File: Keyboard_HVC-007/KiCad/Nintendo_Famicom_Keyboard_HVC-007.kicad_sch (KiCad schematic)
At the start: 96 parts, among them J1 READ/EAR, J2 Conn_01x15, J3 WRITE/MIC, SW1 F8, SW10 @, SW11 ;, SW12 :, SW13 ン, SW14 /, SW15 -, SW16 ^, SW17 F6, SW18 O, SW19 L, SW2 RET, SW20 K, SW21 ,, SW22 ., SW23 P, SW24 0, SW25 F5, SW26 I, SW27 U, SW28 J, SW29 M, SW3 [, SW30 N, SW31 9, SW32 8, SW33 F4, SW34 Y, SW35 G, SW36 H, SW37 B, SW38 V, SW39 7, SW4 ], SW40 6, SW41 F3, SW42 T, SW43 R, SW44 D, SW45 F, SW46 C, SW47 5, SW48 4, SW49 F2, SW5 カナ, SW50 W, SW51 S, SW52 A, SW53 X, SW54 Z, SW55 E, SW56 3, SW57 F1, SW58 ESC, SW59 Q, SW6 RH SHIFT, SW60 CTR, SW61 LH SHIFT, SW62 GRPH, SW63 1, SW64 2, SW65 CLR HOME, SW66 UP, SW67 RIGHT, SW68 LEFT, SW69 DOWN, SW7 ￥, SW70 SPACE, SW71 DEL, SW72 INS, SW8 STOP, SW9 F7, U1 4017, U2 4019, U3 4069

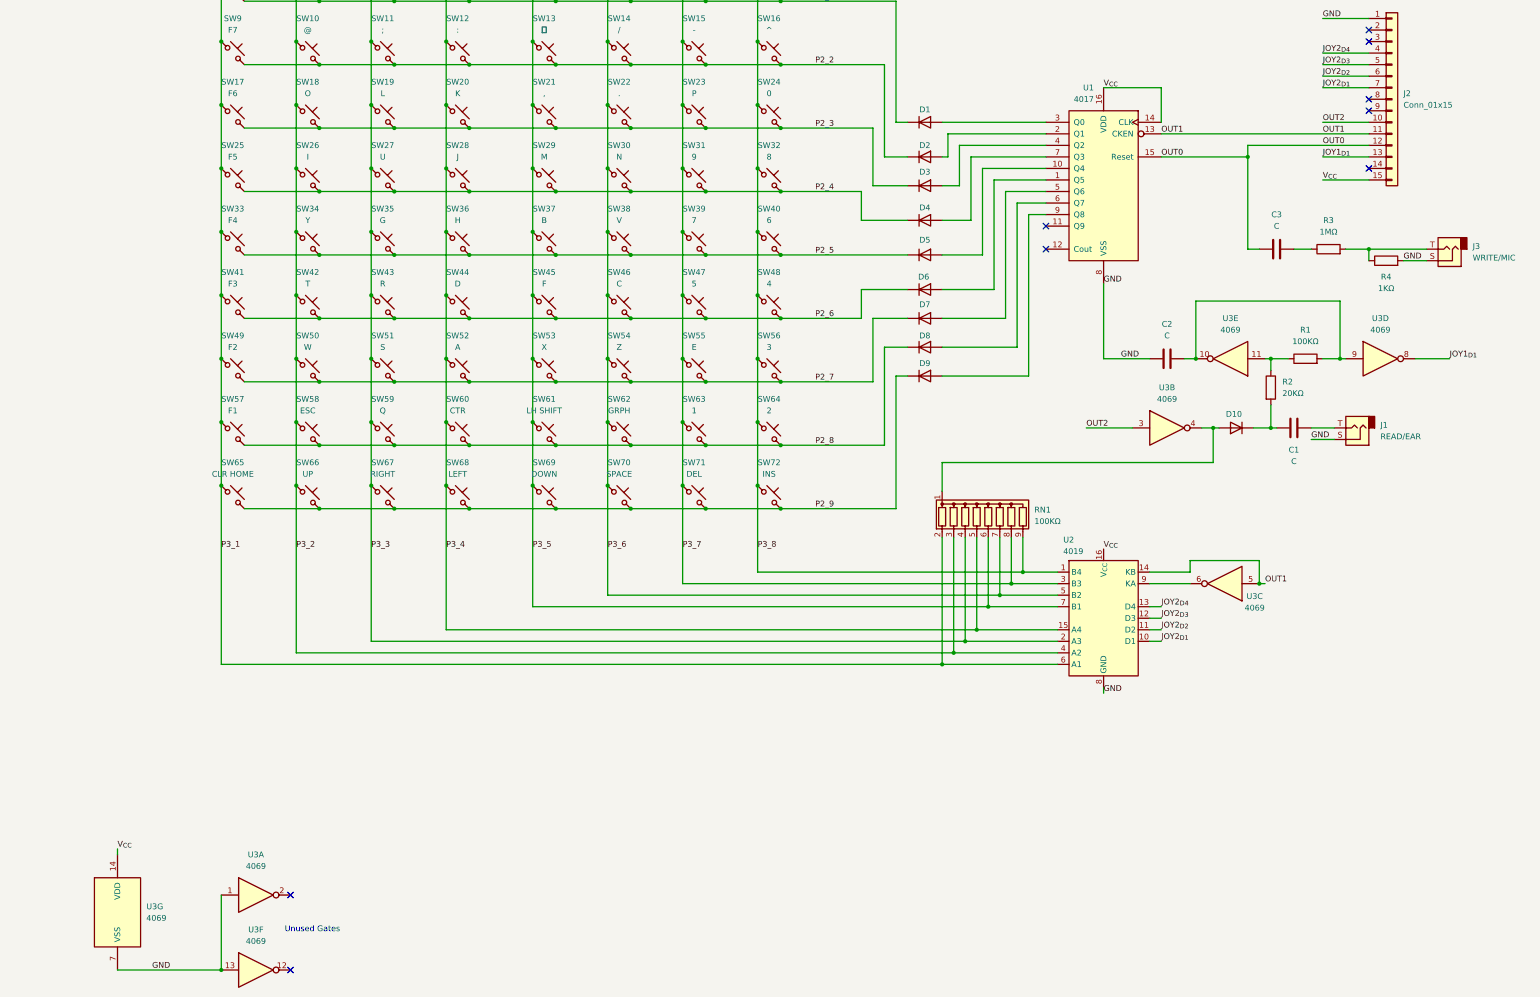
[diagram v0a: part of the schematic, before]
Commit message: Initial keyboard schematic done
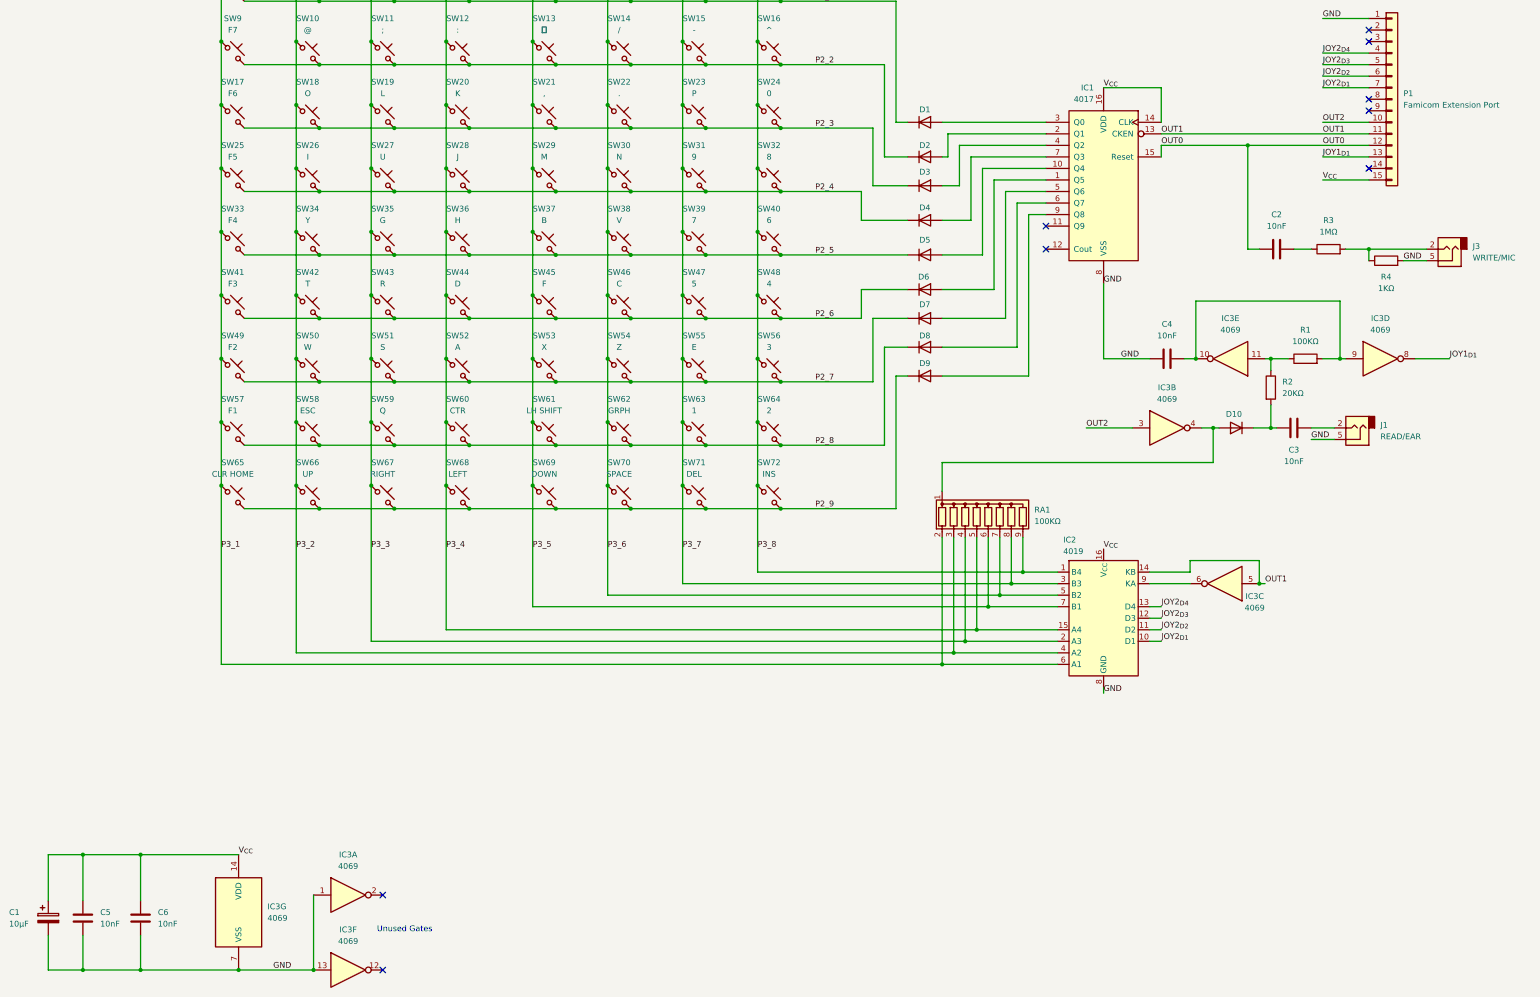
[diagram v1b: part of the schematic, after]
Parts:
- added C1: 10µF, Capacitor_THT:CP_Radial_D5.0mm_P2.50mm, symbol Device:C_Polarized
- added C5, C6: 10nF, Capacitor_THT:C_Axial_L3.8mm_D2.6mm_P7.50mm_Horizontal, symbol Device:C
- C2: renamed from C3; value C -> 10nF; footprint (none) -> Capacitor_THT:C_Axial_L3.8mm_D2.6mm_P7.50mm_Horizontal
- C3: renamed from C1; value C -> 10nF; footprint (none) -> Capacitor_THT:C_Axial_L3.8mm_D2.6mm_P7.50mm_Horizontal
- C4: renamed from C2; value C -> 10nF; footprint (none) -> Capacitor_THT:C_Axial_L3.8mm_D2.6mm_P7.50mm_Horizontal
- D1, D10, D2, D3, D4, D5, D6, D7, D8, D9: footprint (none) -> Diode_THT:D_DO-35_SOD27_P7.62mm_Horizontal
- IC1: renamed from U1; footprint (none) -> Package_DIP:DIP-16_W7.62mm
- IC3: renamed from U3; footprint (none) -> Package_DIP:DIP-16_W7.62mm
- J1, J3: footprint (none) -> Clueless_Engineer:SJ3350820BTR
- P1: renamed from J2; value Conn_01x15 -> Famicom Extension Port; footprint (none) -> Clueless_Engineer:57478374
- R1, R2, R3, R4: footprint (none) -> Resistor_THT:R_Axial_DIN0207_L6.3mm_D2.5mm_P10.16mm_Horizontal
- SW1, SW17, SW2, SW25, SW33, SW41, SW49, SW57, SW6, SW61, SW66, SW67, SW68, SW69, SW9: footprint (none) -> PCM_Switch_Keyboard_Cherry_MX:SW_Cherry_MX_PCB_2.00u
- SW10, SW11, SW12, SW13, SW14, SW15, SW16, SW18, SW19, SW20, SW21, SW22, SW23, SW24, SW26, SW27, SW28, SW29, SW3, SW30, SW31, SW32, SW34, SW35, SW36, SW37, SW38, SW39, SW4, SW40, SW42, SW43, SW44, SW45, SW46, SW47, SW48, SW5, SW50, SW51, SW52, SW53, SW54, SW55, SW56, SW58, SW59, SW60, SW62, SW63, SW64, SW65, SW7, SW71, SW72, SW8: footprint (none) -> PCM_Switch_Keyboard_Cherry_MX:SW_Cherry_MX_PCB_1.00u
- SW70: footprint (none) -> PCM_Switch_Keyboard_Cherry_MX:SW_Cherry_MX_PCB_7.00u
- renumbered U2 to IC2, RN1 to RA1
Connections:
- net GND: now also J1.5, J3.5, C1.2, C5.2, C6.2; no longer J1.S, J3.S
- net V_{CC}: now also C1.1, C5.1, C6.1
- net at R3.2, R4.1: now also J3.2; no longer J3.T
- net at C3.2: now also J1.2; no longer J1.T
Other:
- moved on the sheet: IC3A, IC3F, IC3G

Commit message: PCB design started
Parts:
- IC3: footprint Package_DIP:DIP-16_W7.62mm -> Package_DIP:DIP-14_W7.62mm
- renumbered J1 to P4, J3 to P5
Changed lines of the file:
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@@
 		(dnp no)
 		(fields_autoplaced yes)
-		(property "Reference" "J1"
+		(property "Reference" "P4"
 			(at 321.31 156.8449 0)
 			(effects
@@
 			(project ""
 				(path "/83e19011-2990-4c2b-8979-c23840ecf61d"
-					(reference "J1")
+					(reference "P4")
 					(unit 1)
 				)
@@
 			)
 		)
-		(property "Footprint" "Package_DIP:DIP-16_W7.62mm"
+		(property "Footprint" "Package_DIP:DIP-14_W7.62mm"
 			(at 321.31 142.24 0)
 			(effects
@@
 			)
 		)
-		(property "Footprint" "Package_DIP:DIP-16_W7.62mm"
+		(property "Footprint" "Package_DIP:DIP-14_W7.62mm"
 			(at 69.85 264.16 0)
 			(effects
@@
 		(dnp no)
 		(fields_autoplaced yes)
-		(property "Reference" "J3"
+		(property "Reference" "P5"
 			(at 341.63 117.4749 0)
 			(effects
@@
 			(project ""
 				(path "/83e19011-2990-4c2b-8979-c23840ecf61d"
-					(reference "J3")
+					(reference "P5")
 					(unit 1)
 				)
@@
 			)
 		)
-		(property "Footprint" "Package_DIP:DIP-16_W7.62mm"
+		(property "Footprint" "Package_DIP:DIP-14_W7.62mm"
 			(at 93.98 276.86 0)
 			(effects
@@
 			)
 		)
-		(property "Footprint" "Package_DIP:DIP-16_W7.62mm"
+		(property "Footprint" "Package_DIP:DIP-14_W7.62mm"
 			(at 287.02 191.77 0)
 			(effects
@@
 			)
 		)
-		(property "Footprint" "Package_DIP:DIP-16_W7.62mm"
+		(property "Footprint" "Package_DIP:DIP-14_W7.62mm"
 			(at 274.32 157.48 0)
 			(effects
@@
 			)
 		)
-		(property "Footprint" "Package_DIP:DIP-16_W7.62mm"
+		(property "Footprint" "Package_DIP:DIP-14_W7.62mm"
 			(at 93.98 260.35 0)
 			(effects
@@
 			)
 		)
-		(property "Footprint" "Package_DIP:DIP-16_W7.62mm"
+		(property "Footprint" "Package_DIP:DIP-14_W7.62mm"
 			(at 288.29 142.24 0)
 			(effects

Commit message: PCB design progress
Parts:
- added H1, H2, H3, H4, H5, H6: MountingHole, MountingHole:MountingHole_3.2mm_M3, symbol Mechanical:MountingHole

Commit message: Initial PCB layout completed
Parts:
- removed C1: 10µF, Capacitor_THT:CP_Radial_D5.0mm_P2.50mm, symbol Device:C_Polarized
- added C1: 100nF, Capacitor_THT:C_Axial_L3.8mm_D2.6mm_P7.50mm_Horizontal, symbol Device:C
- added KB1: Space Bar, PCM_Mounting_Keyboard_Stabilizer:Stabilizer_Cherry_MX_7.00u, symbol Clueless_Engineer:Stabiliser
- C5, C6: value 10nF -> 100nF
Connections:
- net GND: now also C1.2
- net V_{CC}: now also C1.1
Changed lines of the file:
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@@
 		(title "Nintendo Famicom Keyboard HVC-007")
 		(date "25/DEC/2025")
-		(rev "WIP")
+		(rev "A")
 		(company "Brett Hallen")
 	)
@@
 	)
 	(symbol
+		(lib_id "Device:C")
+		(at 27.94 265.43 0)
+		(unit 1)
+		(exclude_from_sim no)
+		(in_bom yes)
+		(on_board yes)
+		(dnp no)
+		(property "Reference" "C1"
+			(at 19.304 264.668 0)
+			(effects
+				(font
+					(size 1.27 1.27)
+				)
+				(justify left)
+			)
+		)
+		(property "Value" "100nF"
+			(at 18.542 266.954 0)
+			(effects
+				(font
+					(size 1.27 1.27)
+				)
+				(justify left)
+			)
+		)
+		(property "Footprint" "Capacitor_THT:C_Axial_L3.8mm_D2.6mm_P7.50mm_Horizontal"
+			(at 28.9052 269.24 0)
+			(effects
+				(font
+					(size 1.27 1.27)
+				)
+				(hide yes)
+			)
+		)
+		(property "Datasheet" "~"
+			(at 27.94 265.43 0)
+			(effects
+				(font
+					(size 1.27 1.27)
+				)
+				(hide yes)
+			)
+		)
+		(property "Description" "Unpolarized capacitor"
+			(at 27.94 265.43 0)
+			(effects
+				(font
+					(size 1.27 1.27)
+				)
+				(hide yes)
+			)
+		)
+		(pin "2"
+		)
+		(pin "1"
+		)
+		(instances
+			(project "Nintendo_Famicom_Keyboard_HVC-007"
+				(path "/83e19011-2990-4c2b-8979-c23840ecf61d"
+					(reference "C1")
+					(unit 1)
+				)
+			)
+		)
+	)
+	(symbol
 		(lib_id "Mechanical:MountingHole")
 		(at 378.46 36.83 0)
@@
 			)
 		)
-		(property "Value" "10nF"
+		(property "Value" "100nF"
 			(at 52.07 266.6999 0)
 			(effects
@@
 	)
 	(symbol
-		(lib_id "Device:C_Polarized")
-		(at 27.94 265.43 0)
-		(unit 1)
-		(exclude_from_sim no)
-		(in_bom yes)
-		(on_board yes)
-		(dnp no)
-		(property "Reference" "C1"
-			(at 19.304 264.16 0)
-			(effects
-				(font
-					(size 1.27 1.27)
-				)
-				(justify left)
-			)
-		)
-		(property "Value" "10µF"
-			(at 19.304 266.7 0)
-			(effects
-				(font
-					(size 1.27 1.27)
-				)
-				(justify left)
-			)
-		)
-		(property "Footprint" "Capacitor_THT:CP_Radial_D5.0mm_P2.50mm"
-			(at 28.9052 269.24 0)
-			(effects
-				(font
-					(size 1.27 1.27)
-				)
-				(hide yes)
-			)
-		)
-		(property "Datasheet" "~"
-			(at 27.94 265.43 0)
-			(effects
-				(font
-					(size 1.27 1.27)
-				)
-				(hide yes)
-			)
-		)
-		(property "Description" "Polarized capacitor"
-			(at 27.94 265.43 0)
-			(effects
-				(font
-					(size 1.27 1.27)
-				)
-				(hide yes)
-			)
-		)
-		(pin "2"
-		)
-		(pin "1"
-		)
-		(instances
-			(project ""
-				(path "/83e19011-2990-4c2b-8979-c23840ecf61d"
-					(reference "C1")
-					(unit 1)
-				)
-			)
-		)
-	)
-	(symbol
 		(lib_id "Switch:SW_Push_45deg")
 		(at 85.09 130.81 0)
@@
 			)
 		)
-		(property "Value" "10nF"
+		(property "Value" "100nF"
 			(at 39.37 266.6999 0)
 			(effects
@@
 					(unit 1)
 				)
+			)
+		)
+	)
+	(symbol
+		(lib_id "Clueless_Engineer:Stabiliser")
+		(at 358.14 63.5 0)
+		(unit 1)
+		(exclude_from_sim no)
+		(in_bom yes)
+		(on_board yes)
+		(dnp no)
+		(fields_autoplaced yes)
+		(property "Reference" "KB1"
+			(at 359.41 63.4643 0)
+			(effects
+				(font
+					(size 1.27 1.27)
+				)
+				(justify left)
+			)
+		)
+		(property "Value" "Space Bar"
+			(at 359.41 66.0043 0)
+			(effects
+				(font
+					(size 1.27 1.27)
+				)
+				(justify left)
+			)
+		)
+		(property "Footprint" "PCM_Mounting_Keyboard_Stabilizer:Stabilizer_Cherry_MX_7.00u"
+			(at 358.14 63.5 0)
+			(effects
+				(font
+					(size 1.27 1.27)
+				)
+				(hide yes)
+			)
+		)
+		(property "Datasheet" ""
+			(at 358.14 63.5 0)
+			(effects
+				(font
+					(size 1.27 1.27)
+				)
+				(hide yes)
+			)
+		)
+		(property "Description" ""
+			(at 358.14 63.5 0)
+			(effects
+				(font
+					(size 1.27 1.27)
+				)
+				(hide yes)
+			)
+		)
+		(instances
+			(project ""
+				(path "/83e19011-2990-4c2b-8979-c23840ecf61d"
+					(reference "KB1")
+					(unit 1)
+				)

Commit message: Updated value text visibility
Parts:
- SW2: value RET -> RETURN
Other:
- moved on the sheet: C1, C2, C3, C4, C5, C6, D1, D10, D2, D3, D4, D5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
